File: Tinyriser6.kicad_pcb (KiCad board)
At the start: 4 copper layers, 113.2 x 23.5 mm, 25 parts, among them J1 Bus_M.2_Socket_M, J2 Bus_PCI_Express_x16, J3 Conn_02x04_Odd_Even, J6 USB_A, J7 Conn_01x26_Pin, M1 Fan_4pin

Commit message: little adjustments
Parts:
- moved G*** 1.30 mm to (198.0, 66.7) (x2)
- moved C1 0.95 mm to (140.2, 74.0)
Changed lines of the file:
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@@
 	(footprint "Capacitor_SMD:C_0603_1608Metric"
 		(layer "F.Cu")
-		(at 140.15 73)
+		(at 140.15 73.95)
 		(descr "Capacitor SMD 0603 (1608 Metric), square (rectangular) end terminal, IPC_7351 nominal, (Body size source: IPC-SM-782 page 76, https://www.pcb-3d.com/wordpress/wp-content/uploads/ipc-sm-782a_amendment_1_and_2.pdf), generated with kicad-footprint-generator")
 		(tags "capacitor")
 		(property "Reference" "C1"
-			(at 0 -1.43 0)
+			(at 2.325 0 0)
 			(layer "F.SilkS")
 			(effects
@@
 	(footprint "LOGO"
 		(layer "F.Cu")
-		(at 198.05 68)
+		(at 198.025 66.7)
 		(property "Reference" "G***"
 			(at 0 0 0)
@@
 		(tags "capacitor")
 		(property "Reference" "C3"
-			(at 0 -1.43 90)
+			(at -2.175 0 0)
 			(layer "F.SilkS")
 			(effects
@@
 		(tags "capacitor")
 		(property "Reference" "C2"
-			(at 0 -1.43 0)
+			(at 2.325 -0.01 0)
 			(layer "F.SilkS")
 			(effects
@@
 	(footprint "LOGO"
 		(layer "F.Cu")
-		(at 198.05 68)
+		(at 198.025 66.7)
 		(property "Reference" "G***"
 			(at 0 0 0)
@@
 		(polygon
 			(pts
-				(xy 196.75 66.25) (xy 197.15 65.65) (xy 197.55 66.25) (xy 202.15 66.25) (xy 202.55 65.65) (xy 202.95 66.25)
-				(xy 203.15 66.45) (xy 203.15 69.65) (xy 202.95 69.85) (xy 196.75 69.85) (xy 196.55 69.65) (xy 196.55 66.45)
+				(xy 196.725 64.95) (xy 197.125 64.35) (xy 197.525 64.95) (xy 202.125 64.95) (xy 202.525 64.35) (xy 202.925 64.95)
+				(xy 203.125 65.15) (xy 203.125 68.35) (xy 202.925 68.55) (xy 196.725 68.55) (xy 196.525 68.35) (xy 196.525 65.15)
 			)
 		)

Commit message: Trying to figure out what to do with the random io
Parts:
- removed J7: Conn_01x26_Pin, Connector_PinHeader_2.00mm:PinHeader_2x13_P2.00mm_Vertical
- added J10: Conn_02x04_Odd_Even, Connector_PinHeader_2.00mm:PinHeader_2x04_P2.00mm_Vertical, F.Cu at (174.7, 65.6)
- added J11: Conn_02x04_Odd_Even, Connector_PinHeader_2.00mm:PinHeader_2x04_P2.00mm_Vertical, F.Cu at (178.7, 65.6)
- added J8: Conn_02x04_Odd_Even, Connector_PinHeader_2.00mm:PinHeader_2x04_P2.00mm_Vertical, F.Cu at (166.7, 65.6)
- added J9: Conn_02x04_Odd_Even, Connector_PinHeader_2.00mm:PinHeader_2x04_P2.00mm_Vertical, F.Cu at (170.7, 65.6)
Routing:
- net GPU_PWR_EN: track 0.00 -> 17.6 mm
- net GPU_MACO_EN: track 0.00 -> 16.4 mm
- net PCIe_CPU_REFCLK5-: track 0.00 -> 14.1 mm
- net PCIe_CPU_REFCLK5+: track 0.00 -> 14.1 mm
- net PCIe_CPU_REFCLK11-: track 0.00 -> 14.0 mm
- net PCIe_CPU_REFCLK11+: track 0.00 -> 14.0 mm
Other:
- board text added: "Compatible with Tiny6/Tiny7: Lenovo ThinkCentre M90q Gen 1, M90q Gen 2 Tiny Lenovo ThinkStation P340, P350 Tiny"
- board text added: "TinyRiser6 v1 by WifiCable 2025/xx/xx"
- board text removed: "Compatible with Tiny6: Lenovo ThinkCentre M90q Gen 1, M90q Gen 2 Tiny Lenovo ThinkStation P340, P350 Tiny"
- board text removed: "TinyRiser6 v1 by WifiCable 2025/03/08"

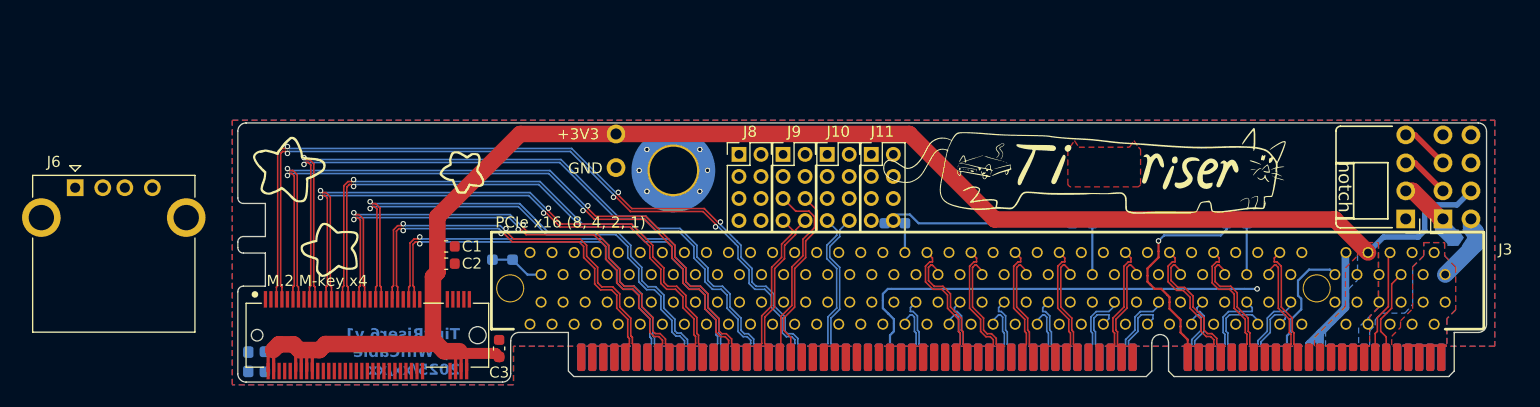
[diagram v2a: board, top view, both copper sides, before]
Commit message: changed usb port, testing new logo placement
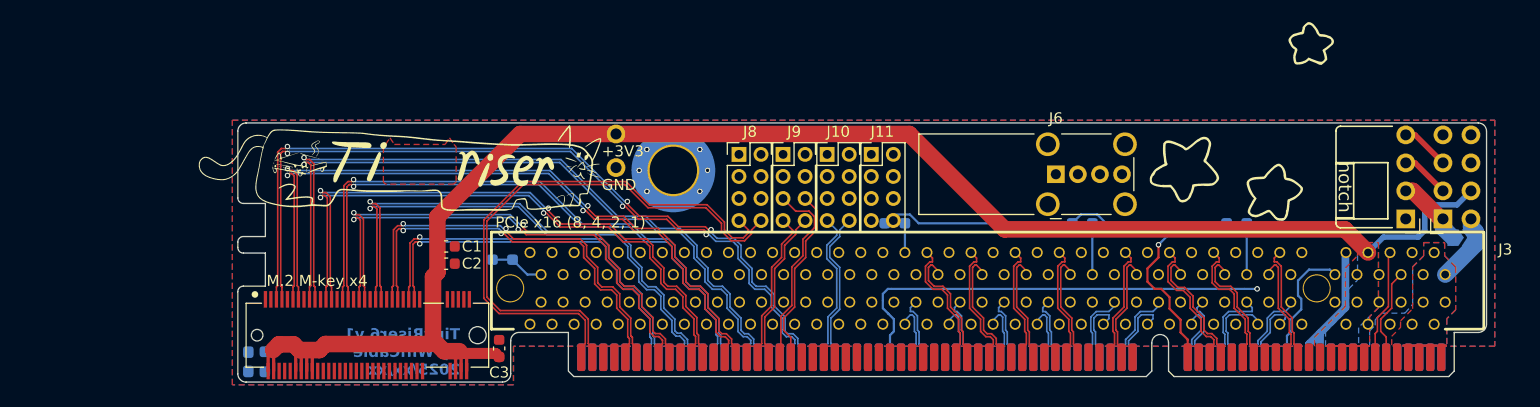
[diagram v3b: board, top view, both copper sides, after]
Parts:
- J6: footprint Connector_USB:USB_A_CONNFLY_DS1095-WNR0 -> Connector_USB:USB_A_Wuerth_614004134726_Horizontal
- moved J6 88.9 mm to (195.4, 67.4)
- moved G*** 81.6 mm to (215.0, 63.6), turned to -135 degrees
- moved G*** 62.1 mm to (135.9, 66.5) (x2)
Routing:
- net PCIe_CPU_REFCLK1+: track 0.00 -> 50.2 mm
- net PCIe_CPU_REFCLK1-: track 0.00 -> 50.2 mm

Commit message: giving up on some random IO pins
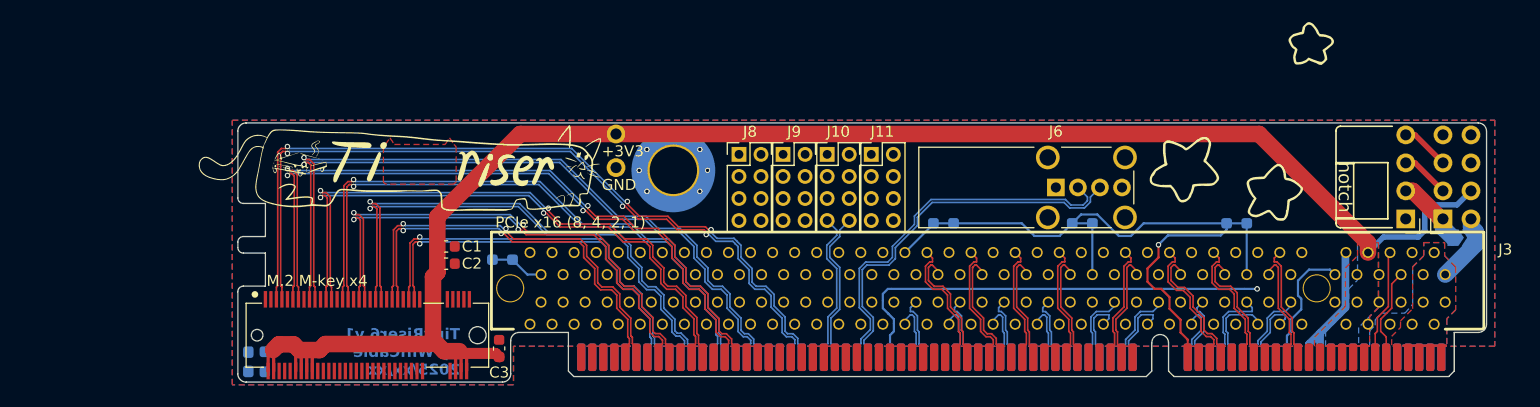
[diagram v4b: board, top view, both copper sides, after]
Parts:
- moved R2 4.41 mm to (185.2, 71.8), turned to 180 degrees
- moved J6 1.20 mm to (195.4, 68.6)
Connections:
- J8 pad 7: PCIe_CPU_REFCLK1- -> unconnected-(J8-Pin_7-Pad7)
- J8 pad 8: PCIe_CPU_REFCLK1+ -> unconnected-(J8-Pin_8-Pad8)
- J9 pad 5: GPU_PWR_EN -> unconnected-(J9-Pin_5-Pad5)
- J9 pad 6: GPU_MACO_EN -> unconnected-(J9-Pin_6-Pad6)
- J9 pad 7: PCIe_CPU_REFCLK5+ -> unconnected-(J9-Pin_7-Pad7)
- J9 pad 8: PCIe_CPU_REFCLK5- -> unconnected-(J9-Pin_8-Pad8)
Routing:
- net PCIe_CPU_REFCLK1+: track 50.2 -> 0.00 mm
- net PCIe_CPU_REFCLK1-: track 50.2 -> 0.00 mm
- net USB_D-: track 0.00 -> 35.2 mm
- net USB_D+: track 0.00 -> 35.2 mm
- net GPU_PWR_EN: track 17.6 -> 0.00 mm
- net GPU_MACO_EN: track 16.4 -> 0.00 mm
- net PCIe_CPU_REFCLK5-: track 14.1 -> 0.00 mm
- net PCIe_CPU_REFCLK5+: track 14.1 -> 0.00 mm
- net PCIe_CPU_CLKREQ#: track 62.6 -> 57.6 mm
- net Net-(J2-~{PRSNT2}-PadB48): track 2.65 -> 3.72 mm
- net +3V3: track 153.3 -> 153.8 mm

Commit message: added todo list
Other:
- board text added: "TODO: [ ] move pcie slot down 0.25mm [ ] change usb footprint [ ] fix logos [ ] somehow make the random io fit"
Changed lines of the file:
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@@
+		)
+	)
+	(gr_text "TODO:\n[ ] move pcie slot down 0.25mm\n[ ] change usb footprint\n[ ] fix logos\n[ ] somehow make the random io fit\n"
+		(at 165.5 108 0)
+		(layer "User.1")
+		(effects
+			(font
+				(size 1.5 1.5)
+				(thickness 0.3)
+				(bold yes)
+			)
+			(justify left bottom)
 		)
 	)

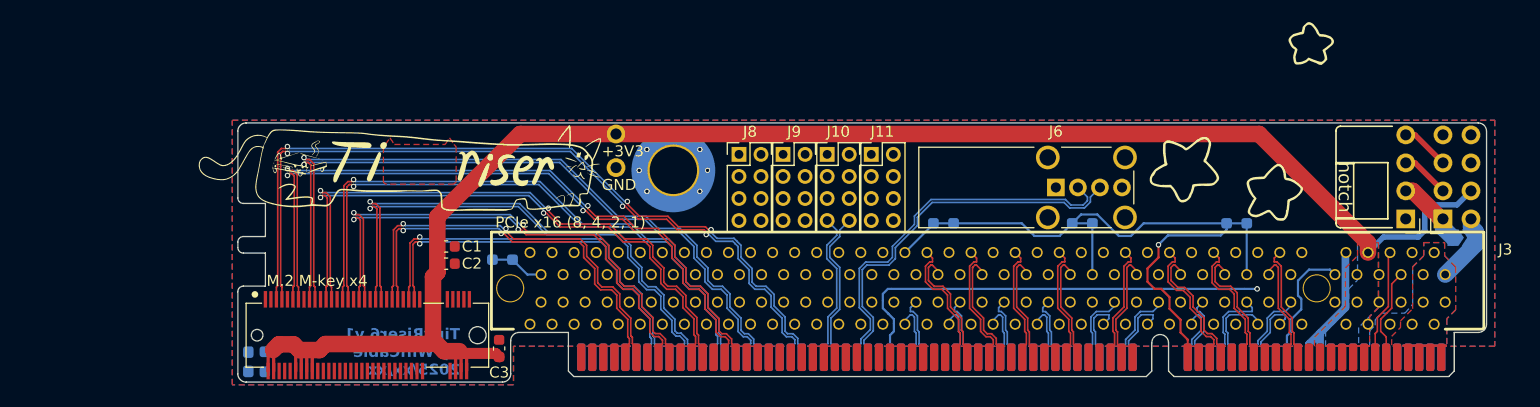
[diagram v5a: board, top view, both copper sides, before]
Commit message: Moved PCIe slot down 0.25mm
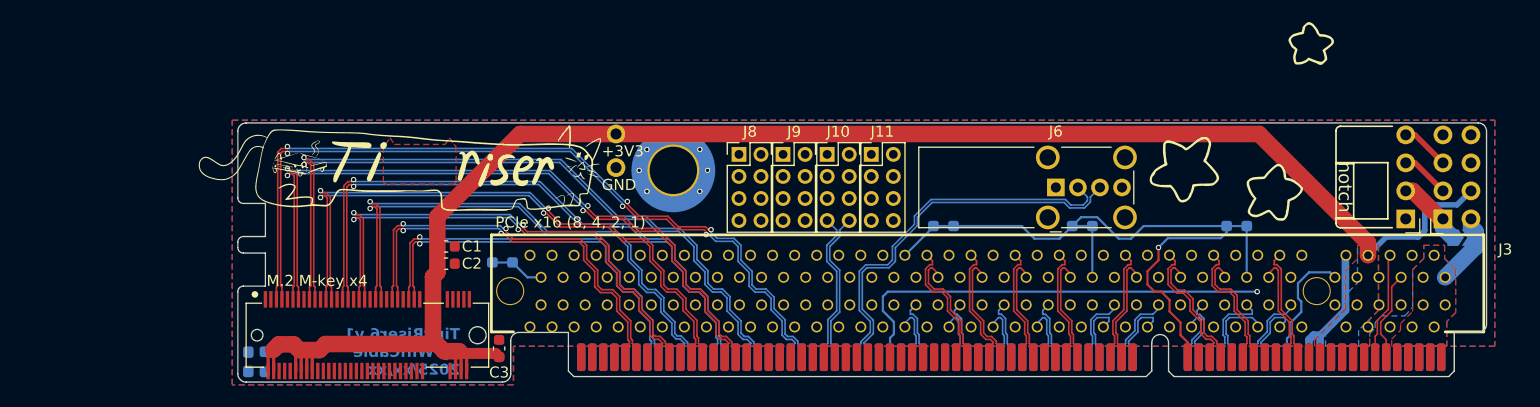
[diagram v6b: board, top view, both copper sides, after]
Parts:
- moved J2 0.25 mm to (189.2, 78.0)
- moved R1 0.25 mm to (145.2, 75.4)
- moved R2 0.25 mm to (185.2, 72.1)
- moved R3 0.25 mm to (197.8, 72.1)
- moved R4 0.25 mm to (211.8, 72.1)
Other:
- board text added: "TODO: [x] move pcie slot down 0.25mm [ ] change usb footprint [ ] fix logos [ ] somehow make the random io fit [ ] look into m.2 slot placement"
- board text removed: "TODO: [ ] move pcie slot down 0.25mm [ ] change usb footprint [ ] fix logos [ ] somehow make the random io fit"

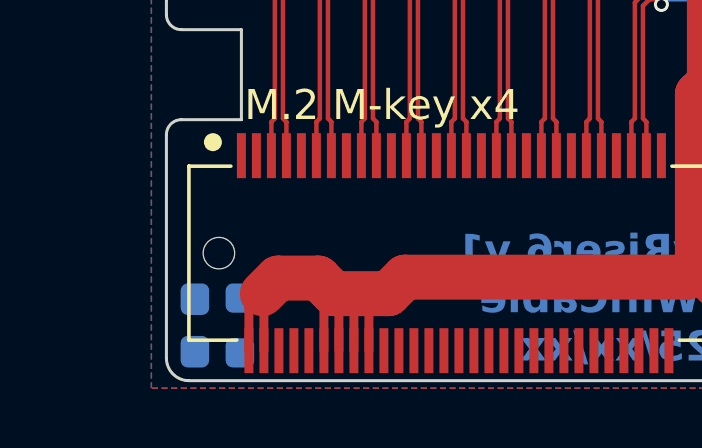
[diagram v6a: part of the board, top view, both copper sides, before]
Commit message: wired up ssd led
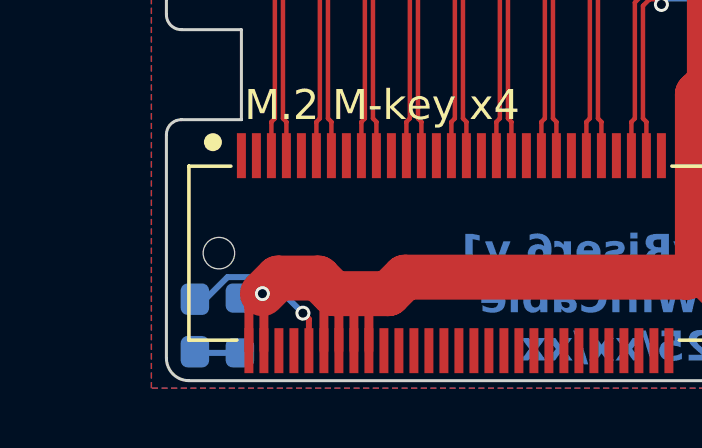
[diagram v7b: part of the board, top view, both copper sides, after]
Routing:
- net Net-(D1-K): track 0.00 -> 5.73 mm, vias 0 -> 1
- net Net-(D1-A): track 0.00 -> 1.52 mm
- net +3V3: track 154.2 -> 155.0 mm, vias 0 -> 1
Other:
- board text added: "TODO: [x] move pcie slot down 0.25mm [ ] change usb footprint [ ] fix logos [ ] somehow make the random io fit [ ] look into m.2 slot placement [ ] ground vias!!!!!!!!!!"
- board text removed: "TODO: [x] move pcie slot down 0.25mm [ ] change usb footprint [ ] fix logos [ ] somehow make the random io fit [ ] look into m.2 slot placement"
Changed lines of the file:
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@@
 		(tags "diode handsolder")
 		(property "Reference" "D1"
-			(at 0 1.43 90)
+			(at 0 1.43 -90)
 			(layer "B.SilkS")
 			(effects
@@
 		)
 		(property "Value" "LED"
-			(at 0 -1.43 90)
+			(at 0 -1.43 -90)
 			(layer "B.Fab")
 			(effects
@@
 			)
 		)
-		(property ki_fp_filters "LED* LED_SMD:* LED_THT:*")
-		(sheetname "Root")
-		(sheetfile "Tinyriser6.kicad_sch")
 		(attr smd)
 		(fp_line
-			(start -1.660001 0.735)
-			(end 0.8 0.735)
-			(stroke
-				(width 0.12)
-				(type solid)
-			)
-			(layer "B.SilkS")
-		)
-		(fp_line
-			(start -1.66 -0.734999)
-			(end -1.660001 0.735)
-			(stroke
-				(width 0.12)
-				(type solid)
-			)
-			(layer "B.SilkS")
-		)
-		(fp_line
-			(start 0.8 -0.735)
-			(end -1.66 -0.734999)
+			(start -1.66 -0.45)
+			(end -1.660001 0.45)
 			(stroke
 				(width 0.12)
@@
 		)
 		(fp_text user "${REFERENCE}"
-			(at 0 0 90)
+			(at 0 0 -90)
 			(layer "B.Fab")
 			(effects
@@
 		)
 	)
-	(gr_text "TODO:\n[x] move pcie slot down 0.25mm\n[ ] change usb footprint\n[ ] fix logos\n[ ] somehow make the random io fit\n[ ] look into m.2 slot placement\n"
-		(at 165.5 108 0)
+	(gr_text "TODO:\n[x] move pcie slot down 0.25mm\n[ ] change usb footprint\n[ ] fix logos\n[ ] somehow make the random io fit\n[ ] look into m.2 slot placement\n[ ] ground vias!!!!!!!!!!"
+		(at 165.5 112.5 0)
 		(layer "User.1")
 		(effects
@@
 		(net 1)
 	)
+	(via
+		(at 124.45 83.35)
+		(size 0.5)
+		(drill 0.3)
+		(layers "F.Cu" "B.Cu")
+		(net 1)
+	)
 	(segment
 		(start 228.3 73.1)
@@
 	)
 	(segment
+		(start 123.7 83.4975)
+		(end 124.3025 83.4975)
+		(width 0.2)
+		(layer "B.Cu")
+		(net 1)
+	)
+	(segment
+		(start 124.3025 83.4975)
+		(end 124.45 83.35)
+		(width 0.2)
+		(layer "B.Cu")
+		(net 1)
+	)
+	(segment
 		(start 233.09 68.91)
 		(end 231.825 70.175)
@@
 	)
 	(segment
+		(start 122.2375 85.3225)
+		(end 122.2 85.285)
+		(width 0.2)
+		(layer "B.Cu")
+		(net 7)
+	)
+	(segment
+		(start 123.7 85.3225)
+		(end 122.2375 85.3225)
+		(width 0.2)
+		(layer "B.Cu")
+		(net 7)
+	)
+	(segment
 		(start 125.925 67.335)
 		(end 126.14408 67.335)
@@
 	)
 	(segment
+		(start 126 85.25)
+		(end 126 84.2)
+		(width 0.2)
+		(layer "F.Cu")
+		(net 132)
+	)
+	(segment
+		(start 126 84.2)
+		(end 125.8 84)
+		(width 0.2)
+		(layer "F.Cu")
+		(net 132)
+	)
+	(via
+		(at 125.8 84)
+		(size 0.5)
+		(drill 0.3)
+		(layers "F.Cu" "B.Cu")
+		(net 132)
+	)
+	(segment
+		(start 123.2847 82.8)
+		(end 122.5497 83.535)
+		(width 0.2)
+		(layer "B.Cu")
+		(net 132)
+	)
+	(segment
+		(start 124.6 82.8)
+		(end 123.2847 82.8)
+		(width 0.2)
+		(layer "B.Cu")
+		(net 132)
+	)
+	(segment
+		(start 122.5497 83.535)
+		(end 122.2 83.535)
+		(width 0.2)
+		(layer "B.Cu")
+		(net 132)
+	)
+	(segment
+		(start 125.8 84)
+		(end 124.6 82.8)
+		(width 0.2)
+		(layer "B.Cu")
+		(net 132)
+	)
+	(segment
